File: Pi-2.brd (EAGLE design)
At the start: 100 x 100 mm, 14 parts, among them IC1 DS18B20, X1 RASPI_GPIO_B+#_PIN, X2 HDD, 5V 700mA, X3 MAC64L

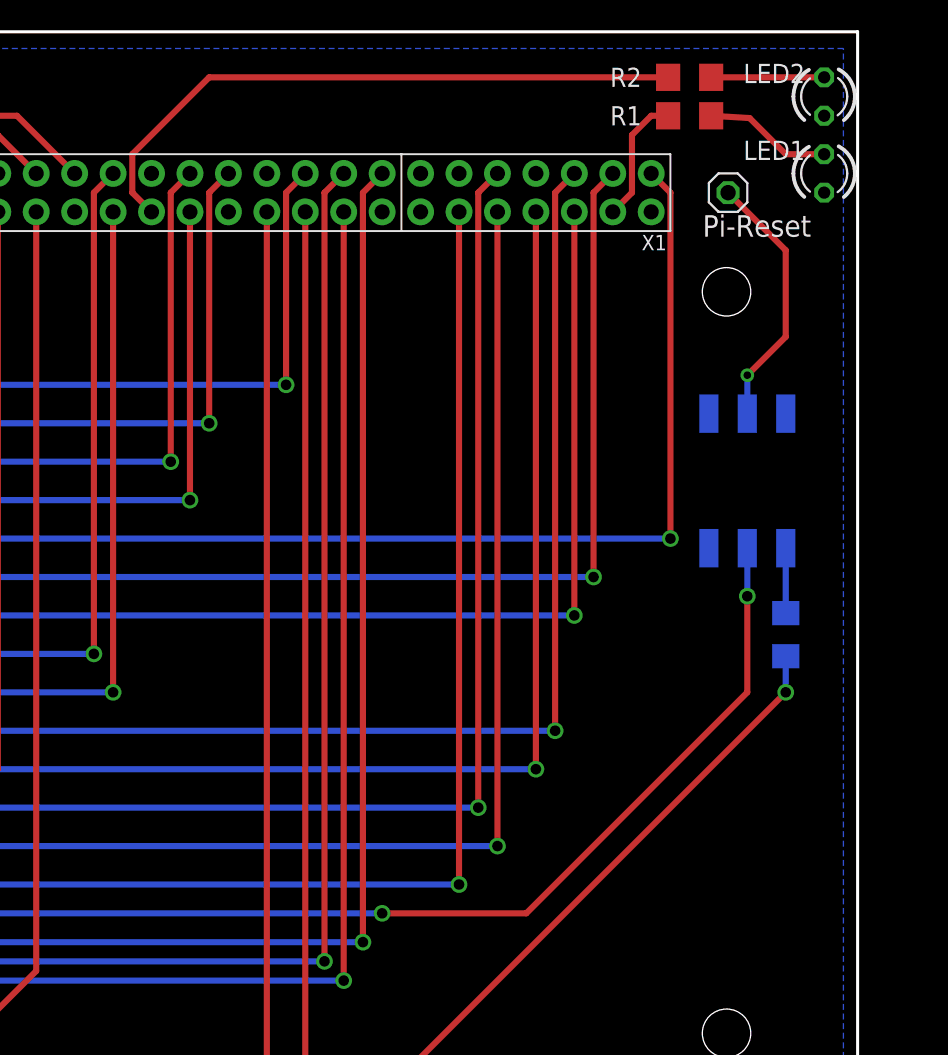
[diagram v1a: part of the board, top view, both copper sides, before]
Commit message: CAN-Bus Beadboard-Adapter, Layouts angepasst
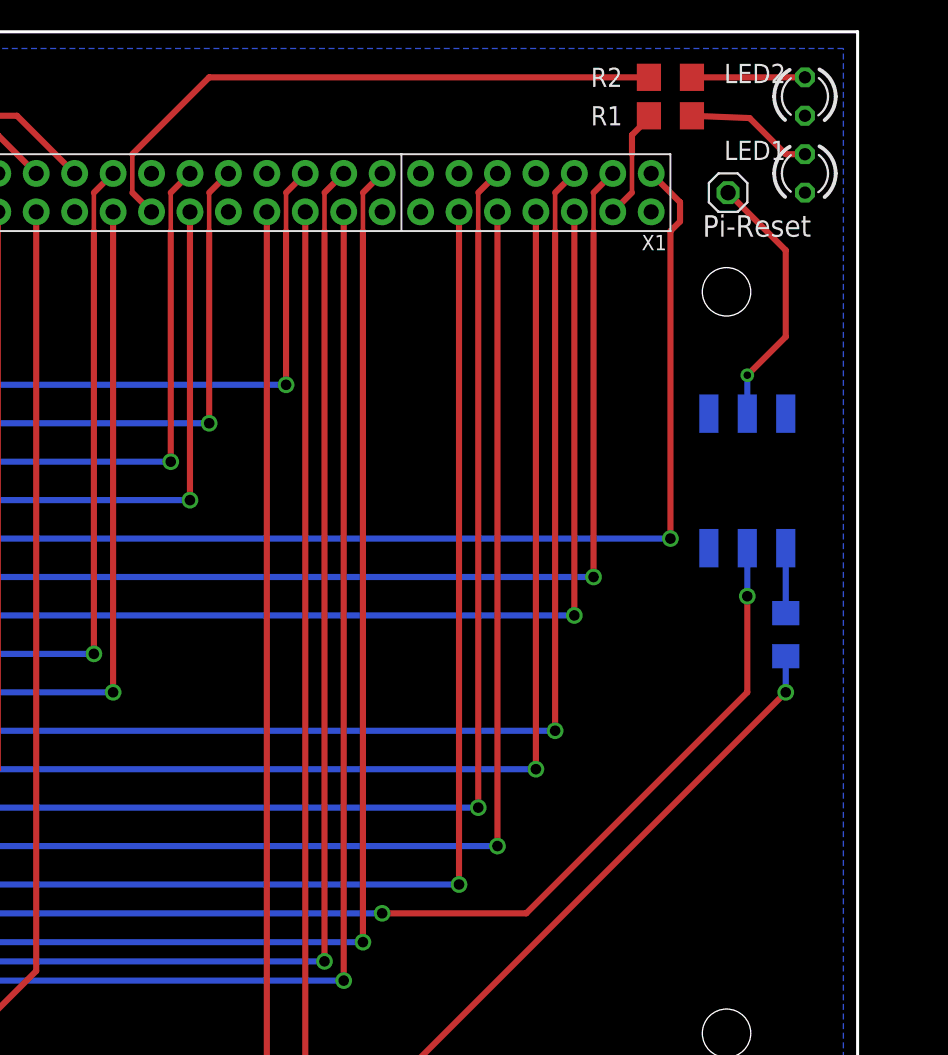
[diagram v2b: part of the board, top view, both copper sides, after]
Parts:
- moved LED1 1.27 mm to (96.5, 90.2)
- moved LED2 1.27 mm to (96.5, 95.2)
- moved R1 1.27 mm to (87.6, 94.0)
- moved R2 1.27 mm to (87.6, 96.5)
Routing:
- net GPIO.27: track 41.8 -> 40.6 mm
- net GPIO.26: track 8.52 -> 7.55 mm
- net GPIO.21: track 102.1 -> 102.7 mm
